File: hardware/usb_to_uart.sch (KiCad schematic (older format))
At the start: 11 parts

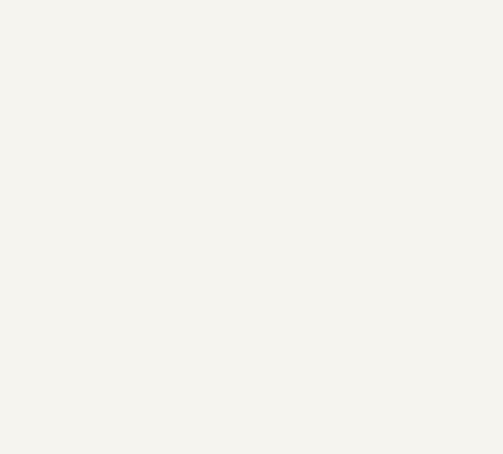
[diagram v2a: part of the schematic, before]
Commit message: update WS2812\,
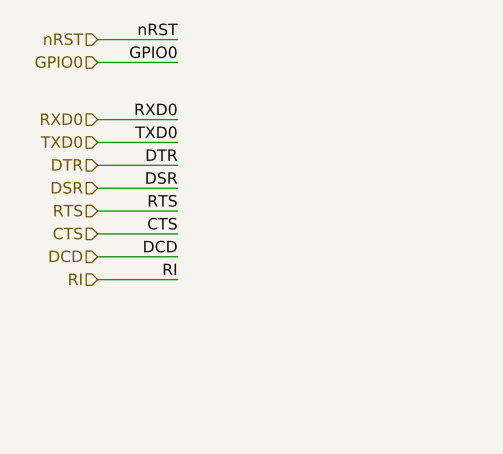
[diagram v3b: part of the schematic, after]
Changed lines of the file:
@@
 $Descr A4 11693 8268
 encoding utf-8
-Sheet 4 11
+Sheet 3 11
 Title ""
 Date ""
@@
 	1    0    0    -1
 $EndComp
+Text Label 1650 700  2    50   ~ 0
+nRST
+Text HLabel 1300 700  0    50   Input ~ 0
+nRST
+Wire Wire Line
+	1650 700  1300 700
+Text Label 1650 800  2    50   ~ 0
+GPIO0
+Text Label 1650 1550 2    50   ~ 0
+CTS
+Text Label 1650 1450 2    50   ~ 0
+RTS
+Text Label 1650 1350 2    50   ~ 0
+DSR
+Text Label 1650 1250 2    50   ~ 0
+DTR
+Text Label 1650 1150 2    50   ~ 0
+TXD0
+Text Label 1650 1050 2    50   ~ 0
+RXD0
+Text Label 1650 1650 2    50   ~ 0
+DCD
+Text Label 1650 1750 2    50   ~ 0
+RI
+Text HLabel 1300 800  0    50   Input ~ 0
+GPIO0
+Wire Wire Line
+	1650 800  1300 800
+Text HLabel 1300 1050 0    50   Input ~ 0
+RXD0
+Text HLabel 1300 1150 0    50   Input ~ 0
+TXD0
+Text HLabel 1300 1250 0    50   Input ~ 0
+DTR
+Text HLabel 1300 1350 0    50   Input ~ 0
+DSR
+Text HLabel 1300 1450 0    50   Input ~ 0
+RTS
+Text HLabel 1300 1650 0    50   Input ~ 0
+DCD
+Text HLabel 1300 1750 0    50   Input ~ 0
+RI
+Text HLabel 1300 1550 0    50   Input ~ 0
+CTS
+Wire Wire Line
+	1300 1050 1650 1050
+Wire Wire Line
+	1300 1150 1650 1150
+Wire Wire Line
+	1300 1250 1650 1250
+Wire Wire Line
+	1300 1350 1650 1350
+Wire Wire Line
+	1300 1450 1650 1450
+Wire Wire Line
+	1300 1550 1650 1550
+Wire Wire Line
+	1300 1650 1650 1650
+Wire Wire Line
+	1300 1750 1650 1750
 $EndSCHEMATC
